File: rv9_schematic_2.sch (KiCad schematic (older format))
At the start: 21 parts

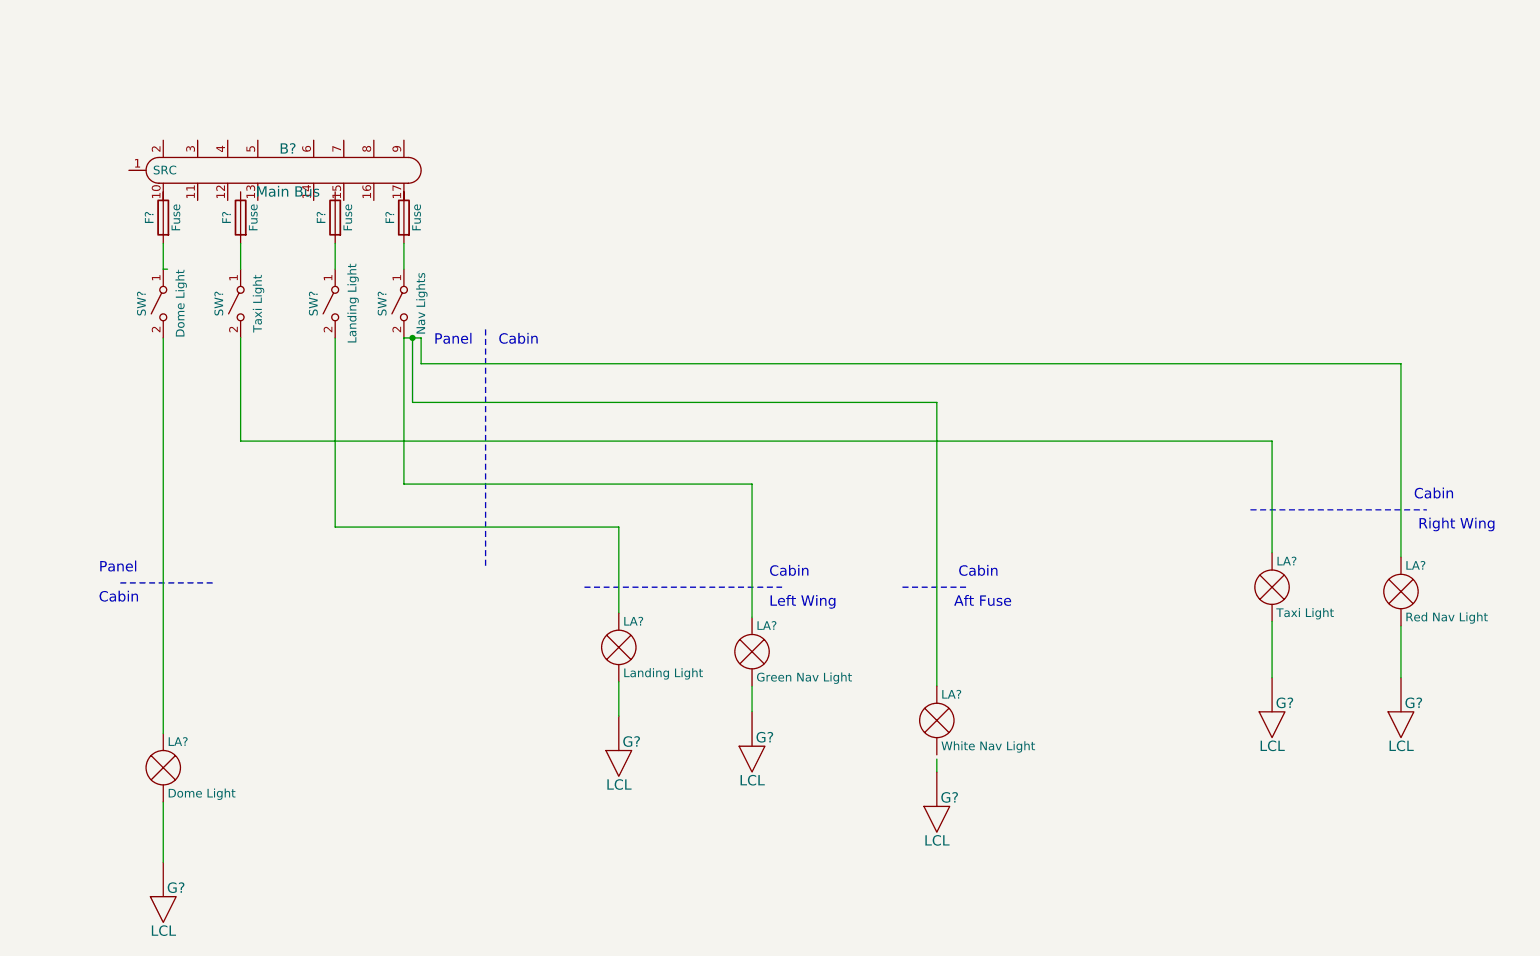
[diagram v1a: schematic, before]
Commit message: Added sheets 3,4,5
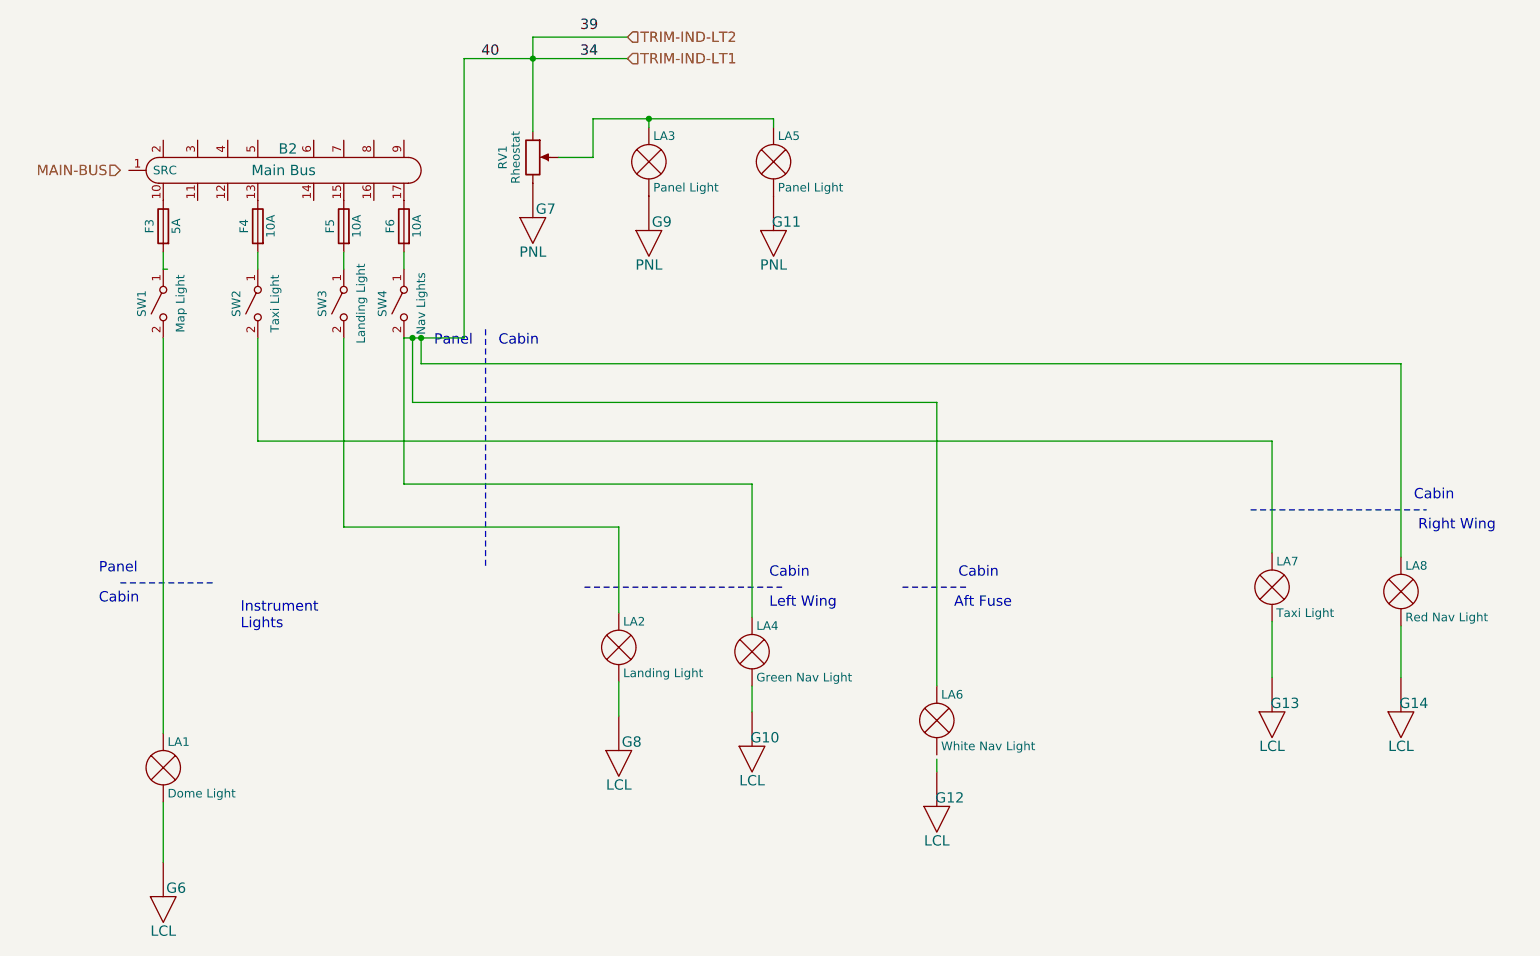
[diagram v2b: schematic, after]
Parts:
- added G11, G7, G9: PNL, symbol LCL
- added LA3, LA5: Panel Light, symbol Lamp
- added RV1: Rheostat, symbol POT
- F3: renamed from F?; value Fuse -> 5A
- F4, F5, F6: renamed from F?; value Fuse -> 10A
- SW1: renamed from SW?; value Dome Light -> Map Light
- gave numbers to parts that had none: 16
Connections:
- net labels added: 34, 39, 40, MAIN-BUS, TRIM-IND-LT1, TRIM-IND-LT2
- wire segments 28 -> 37
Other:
- note added: "Instrument\nLights"
- moved on the sheet: F3, F4, F5, F6, SW2, SW3

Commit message: new version kicad changes
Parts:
- B2: symbol BUS-BAR -> AvionicSchematic:BUS-BAR
- F3, F4, F5, F6: symbol Fuse -> rv_9_schematic-rescue:Fuse
- G10, G11, G12, G13, G14, G6, G7, G8, G9: symbol LCL -> AvionicSchematic:LCL
- LA1, LA2, LA3, LA4, LA5, LA6, LA7, LA8: symbol Lamp -> rv_9_schematic-rescue:Lamp
- RV1: symbol POT -> rv_9_schematic-rescue:POT
- SW1, SW2, SW3, SW4: symbol SW_SPST -> rv_9_schematic-rescue:SW_SPST
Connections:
- wire segments 37 -> 42
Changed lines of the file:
@@
-EESchema Schematic File Version 2
-LIBS:power
-LIBS:device
-LIBS:switches
-LIBS:relays
-LIBS:motors
-LIBS:transistors
-LIBS:conn
-LIBS:linear
-LIBS:regul
-LIBS:74xx
-LIBS:cmos4000
-LIBS:adc-dac
-LIBS:memory
-LIBS:xilinx
-LIBS:microcontrollers
-LIBS:dsp
-LIBS:microchip
-LIBS:analog_switches
-LIBS:motorola
-LIBS:texas
-LIBS:intel
-LIBS:audio
-LIBS:interface
-LIBS:digital-audio
-LIBS:philips
-LIBS:display
-LIBS:cypress
-LIBS:siliconi
-LIBS:opto
-LIBS:atmel
-LIBS:contrib
-LIBS:valves
-LIBS:AvionicSchematic
-LIBS:rv_9_schematic-cache
-EELAYER 25 0
+EESchema Schematic File Version 4
+EELAYER 30 0
 EELAYER END
 $Descr USLetter 11000 8500
@@
 $EndDescr
 $Comp
-L BUS-BAR B2
+L AvionicSchematic:BUS-BAR B2
 U 1 1 5B685BAD
 P 2075 1475
@@
 $EndComp
 $Comp
-L LCL G6
+L AvionicSchematic:LCL G6
 U 1 1 5B685C4C
 P 1350 5775
@@
 $EndComp
 $Comp
-L SW_SPST SW1
+L rv_9_schematic-rescue:SW_SPST SW1
 U 1 1 5B685D35
 P 1350 2250
@@
 $EndComp
 $Comp
-L Fuse F3
+L rv_9_schematic-rescue:Fuse F3
 U 1 1 5B685DEA
 P 1350 1800
+AR Path="/5B685DEA" Ref="F3"  Part="1"
+AR Path="/5B685AE0/5B685DEA" Ref="F3"  Part="1"
 F 0 "F3" V 1430 1800 50  0000 C CNN
 F 1 "5A" V 1275 1800 50  0000 C CNN
@@
 $EndComp
 $Comp
-L Lamp LA4
+L rv_9_schematic-rescue:Lamp LA4
 U 1 1 5B685EA7
 P 4775 4275
@@
 $EndComp
 $Comp
-L Fuse F4
+L rv_9_schematic-rescue:Fuse F4
 U 1 1 5B686382
 P 1900 1800
+AR Path="/5B686382" Ref="F4"  Part="1"
+AR Path="/5B685AE0/5B686382" Ref="F4"  Part="1"
 F 0 "F4" V 1980 1800 50  0000 C CNN
 F 1 "10A" V 1825 1800 50  0000 C CNN
@@
 $EndComp
 $Comp
-L Fuse F5
+L rv_9_schematic-rescue:Fuse F5
 U 1 1 5B6863BE
 P 2400 1800
+AR Path="/5B6863BE" Ref="F5"  Part="1"
+AR Path="/5B685AE0/5B6863BE" Ref="F5"  Part="1"
 F 0 "F5" V 2480 1800 50  0000 C CNN
 F 1 "10A" V 2325 1800 50  0000 C CNN
@@
 $EndComp
 $Comp
-L Fuse F6
+L rv_9_schematic-rescue:Fuse F6
 U 1 1 5B6863FB
 P 2750 1800
+AR Path="/5B6863FB" Ref="F6"  Part="1"
+AR Path="/5B685AE0/5B6863FB" Ref="F6"  Part="1"
 F 0 "F6" V 2830 1800 50  0000 C CNN
 F 1 "10A" V 2675 1800 50  0000 C CNN
@@
 $EndComp
 $Comp
-L SW_SPST SW2
+L rv_9_schematic-rescue:SW_SPST SW2
 U 1 1 5B686C5D
 P 1900 2250
@@
 $EndComp
 $Comp
-L SW_SPST SW3
+L rv_9_schematic-rescue:SW_SPST SW3
 U 1 1 5B686CAE
 P 2400 2250
@@
 $EndComp
 $Comp
-L SW_SPST SW4
+L rv_9_schematic-rescue:SW_SPST SW4
 U 1 1 5B686CF6
 P 2750 2250
@@
 	2750 1950 2750 2050
 $Comp
-L Lamp LA8
+L rv_9_schematic-rescue:Lamp LA8
 U 1 1 5B6875D4
 P 8550 3925
@@
 $EndComp
 $Comp
-L Lamp LA6
+L rv_9_schematic-rescue:Lamp LA6
 U 1 1 5B68764C
 P 5850 4675
@@
 	4775 3300 4775 4075
 Wire Wire Line
-	2750 2450 3100 2450
+	2750 2450 2800 2450
 Wire Wire Line
 	2800 2450 2800 2825
@@
 Connection ~ 2800 2450
 $Comp
-L LCL G10
+L AvionicSchematic:LCL G10
 U 1 1 5B6879B3
 P 4775 4900
@@
 $EndComp
 $Comp
-L LCL G14
+L AvionicSchematic:LCL G14
 U 1 1 5B687C95
 P 8550 4700
@@
 $EndComp
 $Comp
-L LCL G12
+L AvionicSchematic:LCL G12
 U 1 1 5B687D12
 P 5850 5250
@@
 	5850 4900 5850 4975
 $Comp
-L Lamp LA2
+L rv_9_schematic-rescue:Lamp LA2
 U 1 1 5B688FD7
 P 4000 4250
@@
 $EndComp
 $Comp
-L Lamp LA7
+L rv_9_schematic-rescue:Lamp LA7
 U 1 1 5B6890D4
 P 7800 3900
@@
 	7800 3050 7800 3700
 $Comp
-L Lamp LA1
+L rv_9_schematic-rescue:Lamp LA1
 U 1 1 5B689464
 P 1350 4950
@@
 	1350 2450 1350 4750
 $Comp
-L LCL G13
+L AvionicSchematic:LCL G13
 U 1 1 5B68A056
 P 7800 4700
@@
 $EndComp
 $Comp
-L LCL G8
+L AvionicSchematic:LCL G8
 U 1 1 5B68A3B4
 P 4000 4925
@@
 Instrument\nLights
 Wire Wire Line
-	3500 700  3500 1250
-Wire Wire Line
-	3100 825  4050 825
+	3500 700  3500 825
+Wire Wire Line
+	3100 825  3500 825
 Wire Wire Line
 	3500 700  4050 700
@@
 34
 $Comp
-L Lamp LA3
+L rv_9_schematic-rescue:Lamp LA3
 U 1 1 5B7A9B14
 P 4175 1425
@@
 $EndComp
 $Comp
-L Lamp LA5
+L rv_9_schematic-rescue:Lamp LA5
 U 1 1 5B7A9BEE
 P 4900 1425
@@
 	4900 1175 4900 1225
 $Comp
-L LCL G9
+L AvionicSchematic:LCL G9
 U 1 1 5B7AC223
 P 4175 1900
@@
 $EndComp
 $Comp
-L LCL G11
+L AvionicSchematic:LCL G11
 U 1 1 5B7AC34B
 P 4900 1900
@@
 $EndComp
 $Comp
-L POT RV1
+L rv_9_schematic-rescue:POT RV1
 U 1 1 5B7AC93A
 P 3500 1400
@@
 $EndComp
 $Comp
-L LCL G7
+L AvionicSchematic:LCL G7
 U 1 1 5B7ACAFA
 P 3500 1825
@@
 	3850 1400 3850 1175
 Wire Wire Line
-	3850 1175 4900 1175
+	3850 1175 4175 1175
 Connection ~ 4175 1175
 Text Label 3200 825  0    60   ~ 0
@@
 Text HLabel 1100 1475 0    60   Input ~ 0
 MAIN-BUS
+Wire Wire Line
+	2800 2450 2850 2450
+Wire Wire Line
+	3500 825  3500 1250
+Wire Wire Line
+	3500 825  4050 825
+Wire Wire Line
+	2850 2450 3100 2450
+Wire Wire Line
+	4175 1175 4900 1175
 $EndSCHEMATC
